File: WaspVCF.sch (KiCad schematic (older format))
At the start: 15 parts

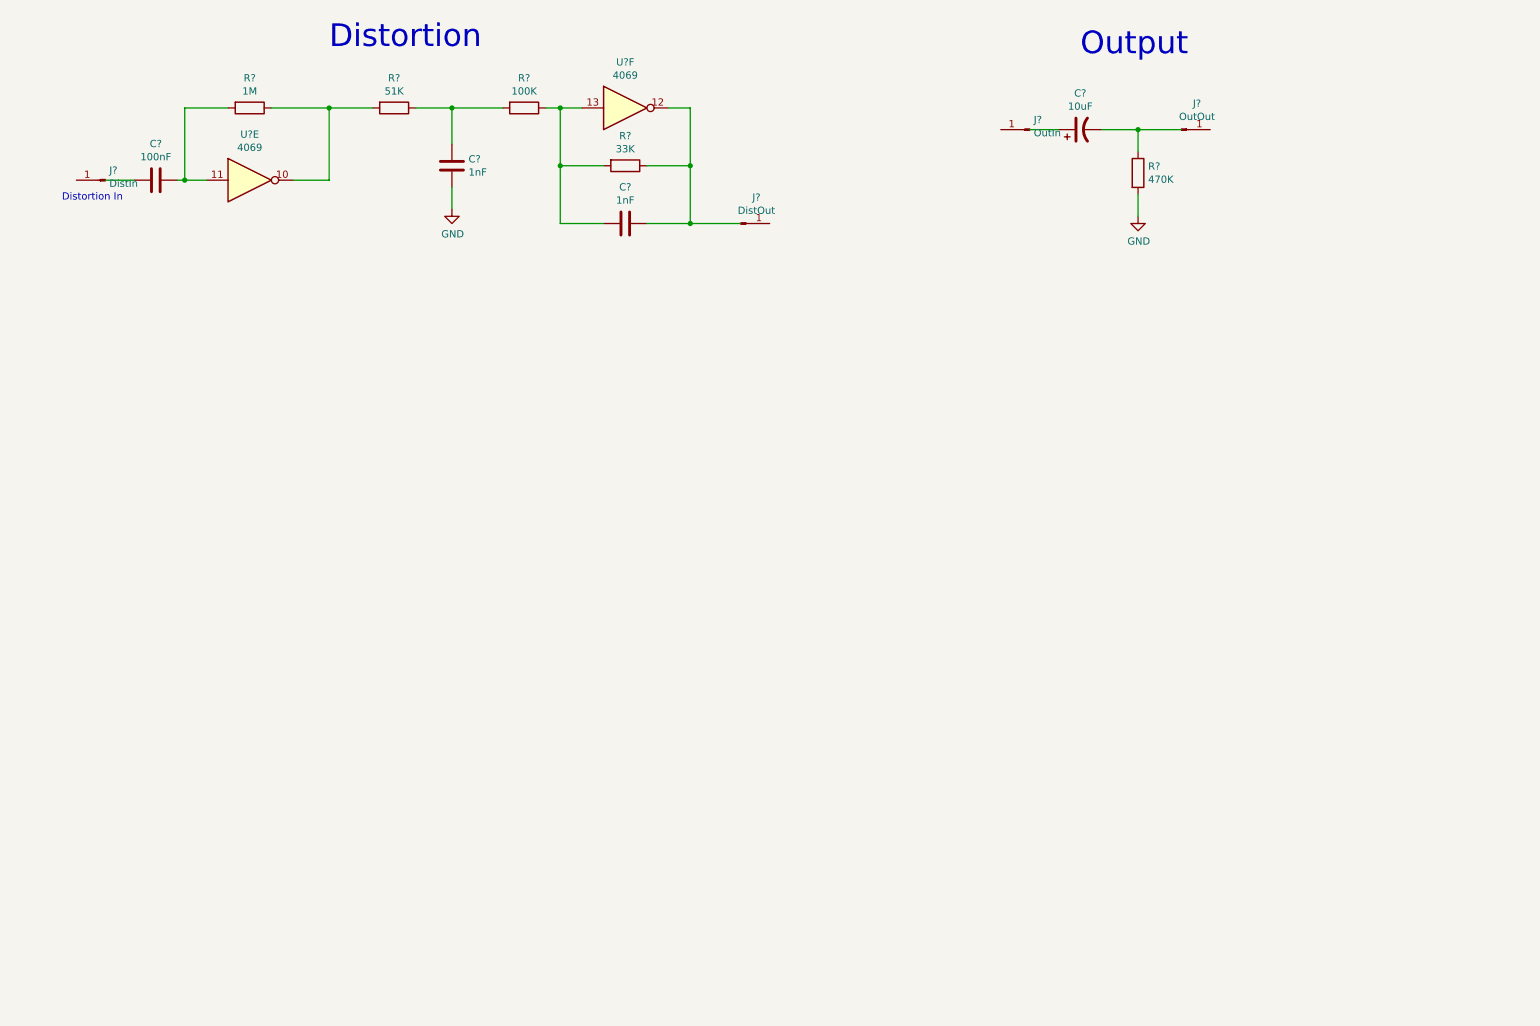
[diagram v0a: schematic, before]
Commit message: Completed Schematic
Annotations and ERC done
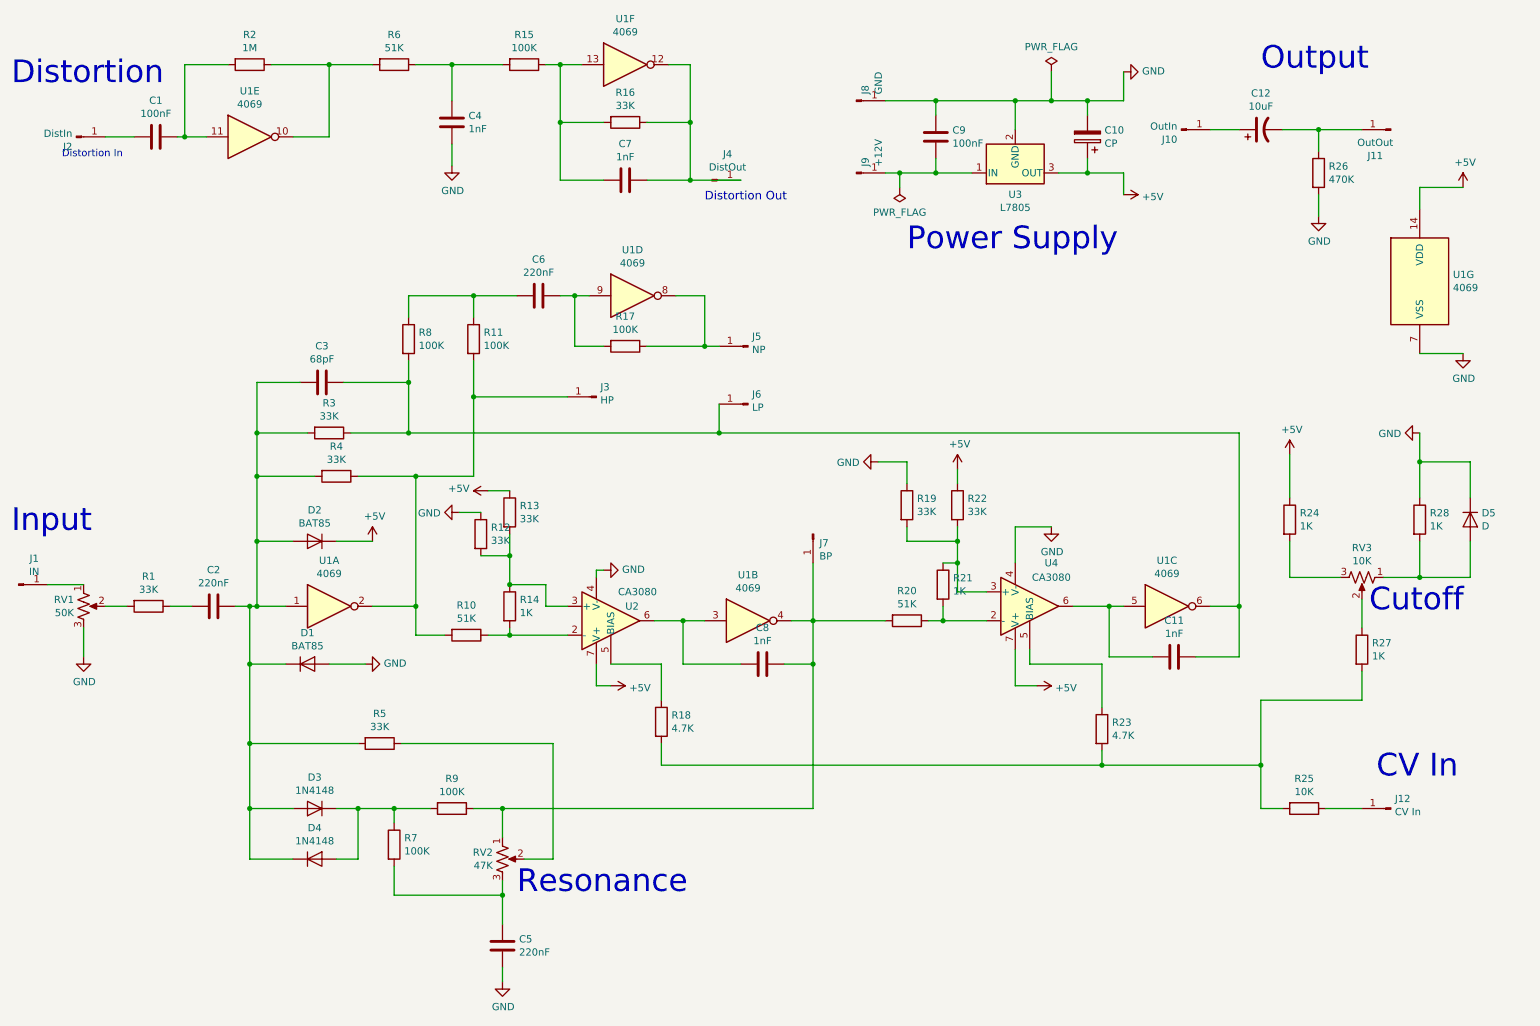
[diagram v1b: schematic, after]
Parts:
- added C10: CP, symbol Device:CP
- added C11, C8: 1nF, symbol Device:C
- added C2, C5, C6: 220nF, symbol Device:C
- added C3: 68pF, symbol Device:C
- added C9: 100nF, symbol Device:C
- added D1, D2: BAT85, symbol Device:D
- added D3, D4: 1N4148, symbol Device:D
- added D5: D, symbol Device:D
- added J1: IN, symbol Connector:Conn_01x01_Male
- added J12: CV In, symbol Connector:Conn_01x01_Male
- added J3: HP, symbol Connector:Conn_01x01_Male
- added J5: NP, symbol Connector:Conn_01x01_Male
- added J6: LP, symbol Connector:Conn_01x01_Male
- added J7: BP, symbol Connector:Conn_01x01_Male
- added J8: GND, symbol Connector:Conn_01x01_Male
- added J9: +12V, symbol Connector:Conn_01x01_Male
- added R1, R12, R13, R19, R22, R3, R4, R5: 33K, symbol Device:R
- added R10, R20: 51K, symbol Device:R
- added R11, R17, R7, R8, R9: 100K, symbol Device:R
- added R14, R21, R24, R27, R28: 1K, symbol Device:R
- added R18, R23: 4.7K, symbol Device:R
- added R25: 10K, symbol Device:R
- added RV1: 50K, symbol Device:R_POT_US
- added RV2: 47K, symbol Device:R_POT_US
- added RV3: 10K, symbol Device:R_POT_US
- added unit 1 of U1
- added unit 4 of U1
- added unit 3 of U1
- added unit 2 of U1
- added unit 7 of U1
- added U2, U4: CA3080, symbol Amplifier_Operational:CA3080
- added U3: L7805, symbol Regulator_Linear:L7805
- gave numbers to parts that had none: 14
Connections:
- net labels added: +5V
- wire segments 30 -> 199
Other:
- note added: "CV In"
- note added: "Cutoff"
- note added: "Distortion Out"
- note added: "Input"
- note added: "Power Supply"
- note added: "Resonance"
- moved on the sheet: C1, C12, C4, C7, J10, J11, J2, J4, R15, R16, R2, R26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

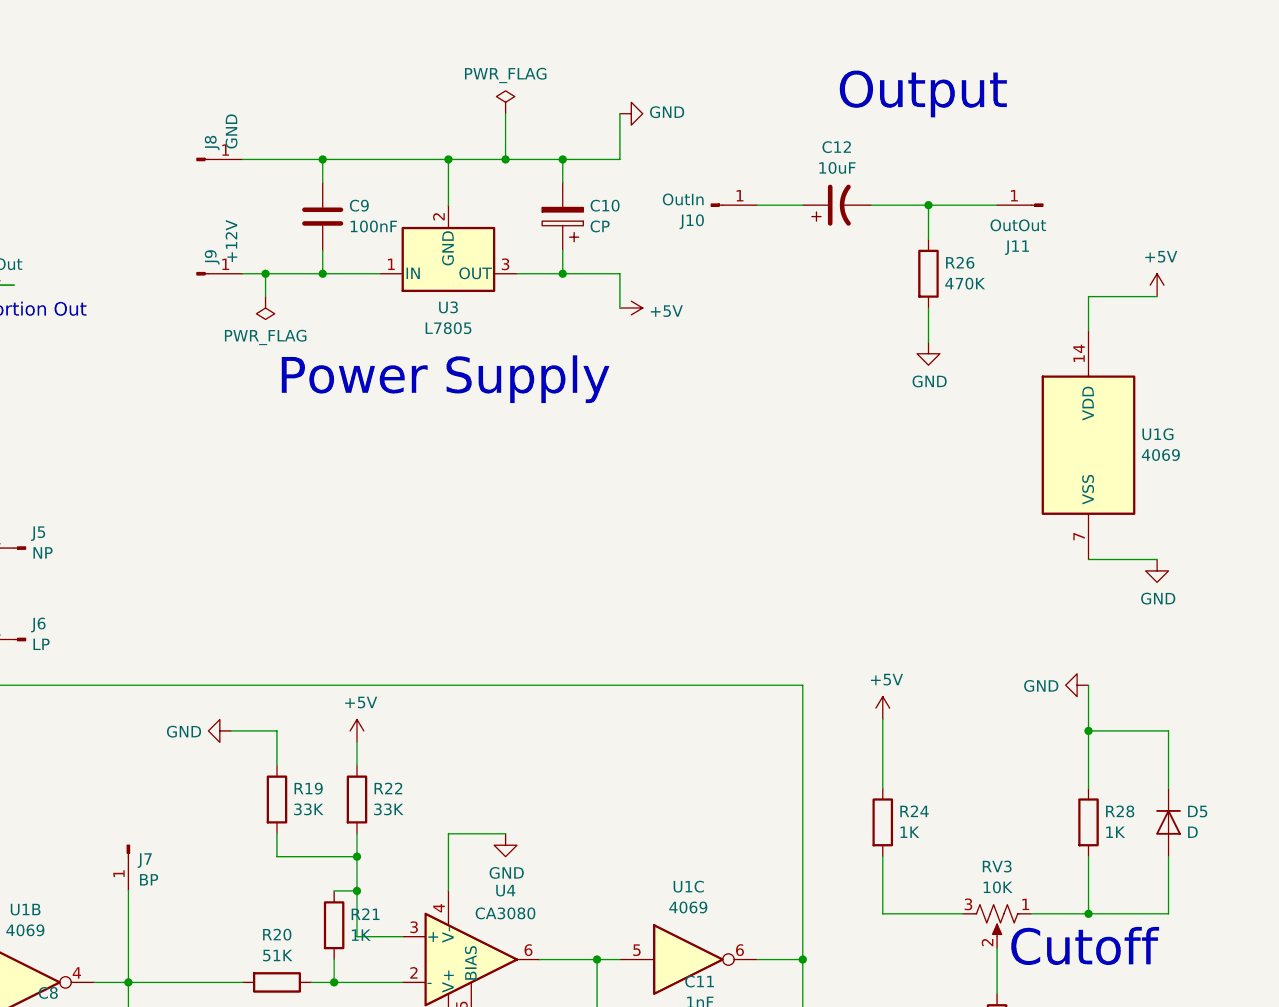
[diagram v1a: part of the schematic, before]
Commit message: Assigned Footprints
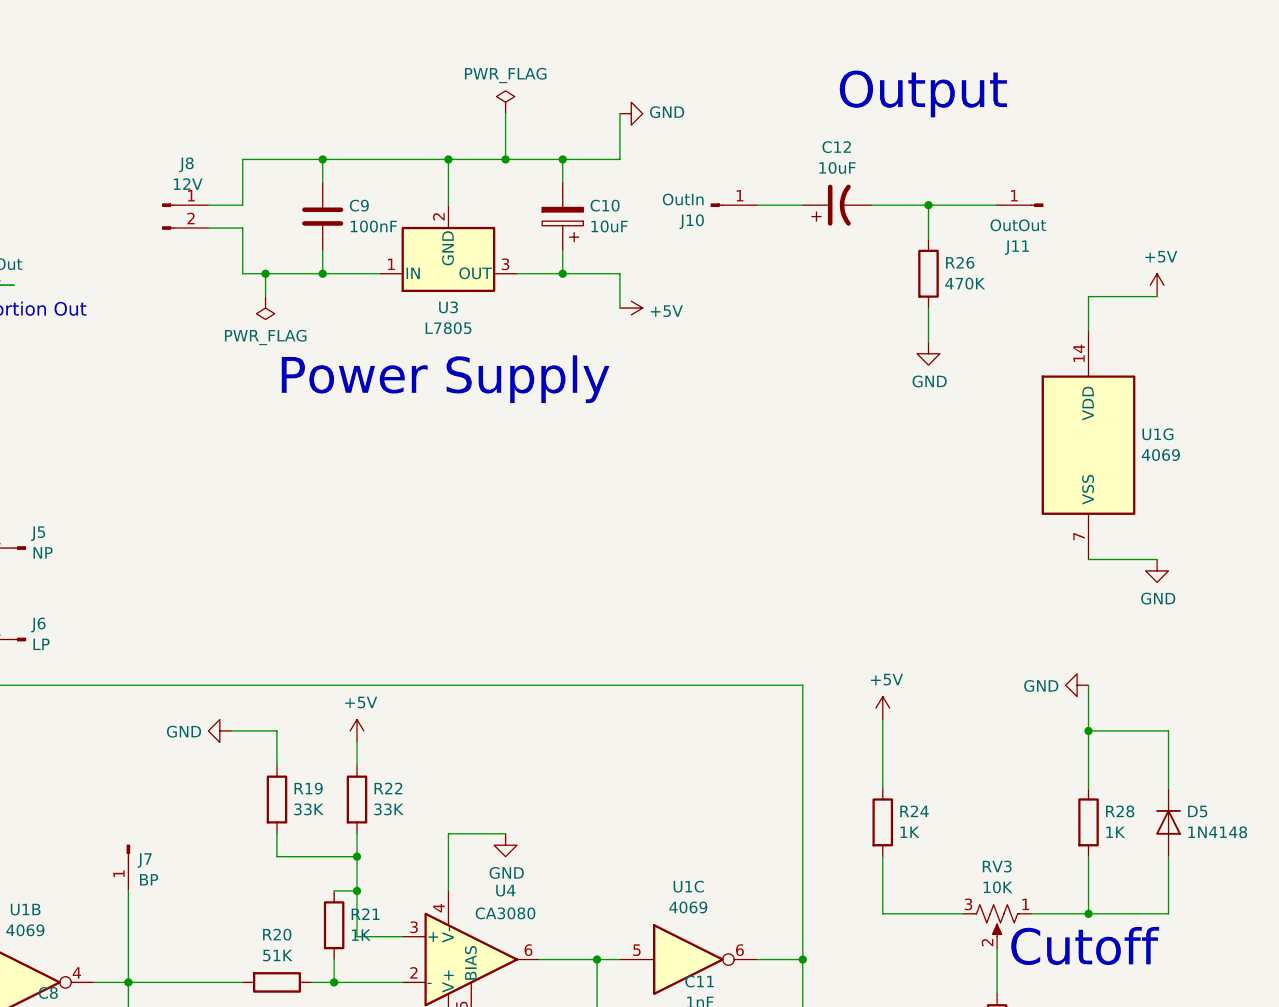
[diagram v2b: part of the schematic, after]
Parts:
- removed J8: GND, symbol Connector:Conn_01x01_Male
- removed J9: +12V, symbol Connector:Conn_01x01_Male
- added J8: 12V, Pin_Headers:Pin_Header_Straight_1x02_Pitch2.54mm, symbol Connector:Conn_01x02_Male
- C1, C11, C2, C3, C4, C5, C6, C7, C8, C9: footprint (none) -> Capacitors_ThroughHole:C_Disc_D6.0mm_W2.5mm_P5.00mm
- C10: value CP -> 10uF; footprint (none) -> Capacitors_ThroughHole:CP_Radial_D5.0mm_P2.50mm
- C12: footprint (none) -> Capacitors_ThroughHole:CP_Radial_D5.0mm_P2.50mm
- D1, D2, D3, D4: footprint (none) -> Diodes_ThroughHole:D_T-1_P5.08mm_Horizontal
- D5: value D -> 1N4148; footprint (none) -> Diodes_ThroughHole:D_T-1_P5.08mm_Horizontal
- J1, J10, J11, J12, J2, J3, J4, J5, J6, J7: footprint (none) -> Pin_Headers:Pin_Header_Straight_1x01_Pitch2.54mm
- R1, R10, R11, R12, R13, R14, R15, R16, R17, R18, R19, R2, R20, R21, R22, R23, R24, R25, R26, R27, R28, R3, R4, R5, R6, R7, R8, R9: footprint (none) -> Resistors_ThroughHole:R_Axial_DIN0207_L6.3mm_D2.5mm_P7.62mm_Horizontal
- RV1, RV2, RV3: footprint (none) -> Pin_Headers:Pin_Header_Straight_1x03_Pitch2.54mm
- U1: footprint (none) -> Housings_DIP:DIP-14_W7.62mm_Socket_LongPads
- U2: footprint (none) -> Housings_DIP:DIP-8_W7.62mm_Socket_LongPads
- U3: footprint (none) -> TO_SOT_Packages_THT:TO-220-3_Vertical
- U4: footprint (none) -> Housings_DIP:DIP-8_W7.62mm_LongPads
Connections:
- net GND: now also J8.1 (Pin_1)
- net at C9.2, U3.1 (IN): now also J8.2 (Pin_2)
